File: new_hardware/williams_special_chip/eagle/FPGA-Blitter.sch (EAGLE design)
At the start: 3 parts

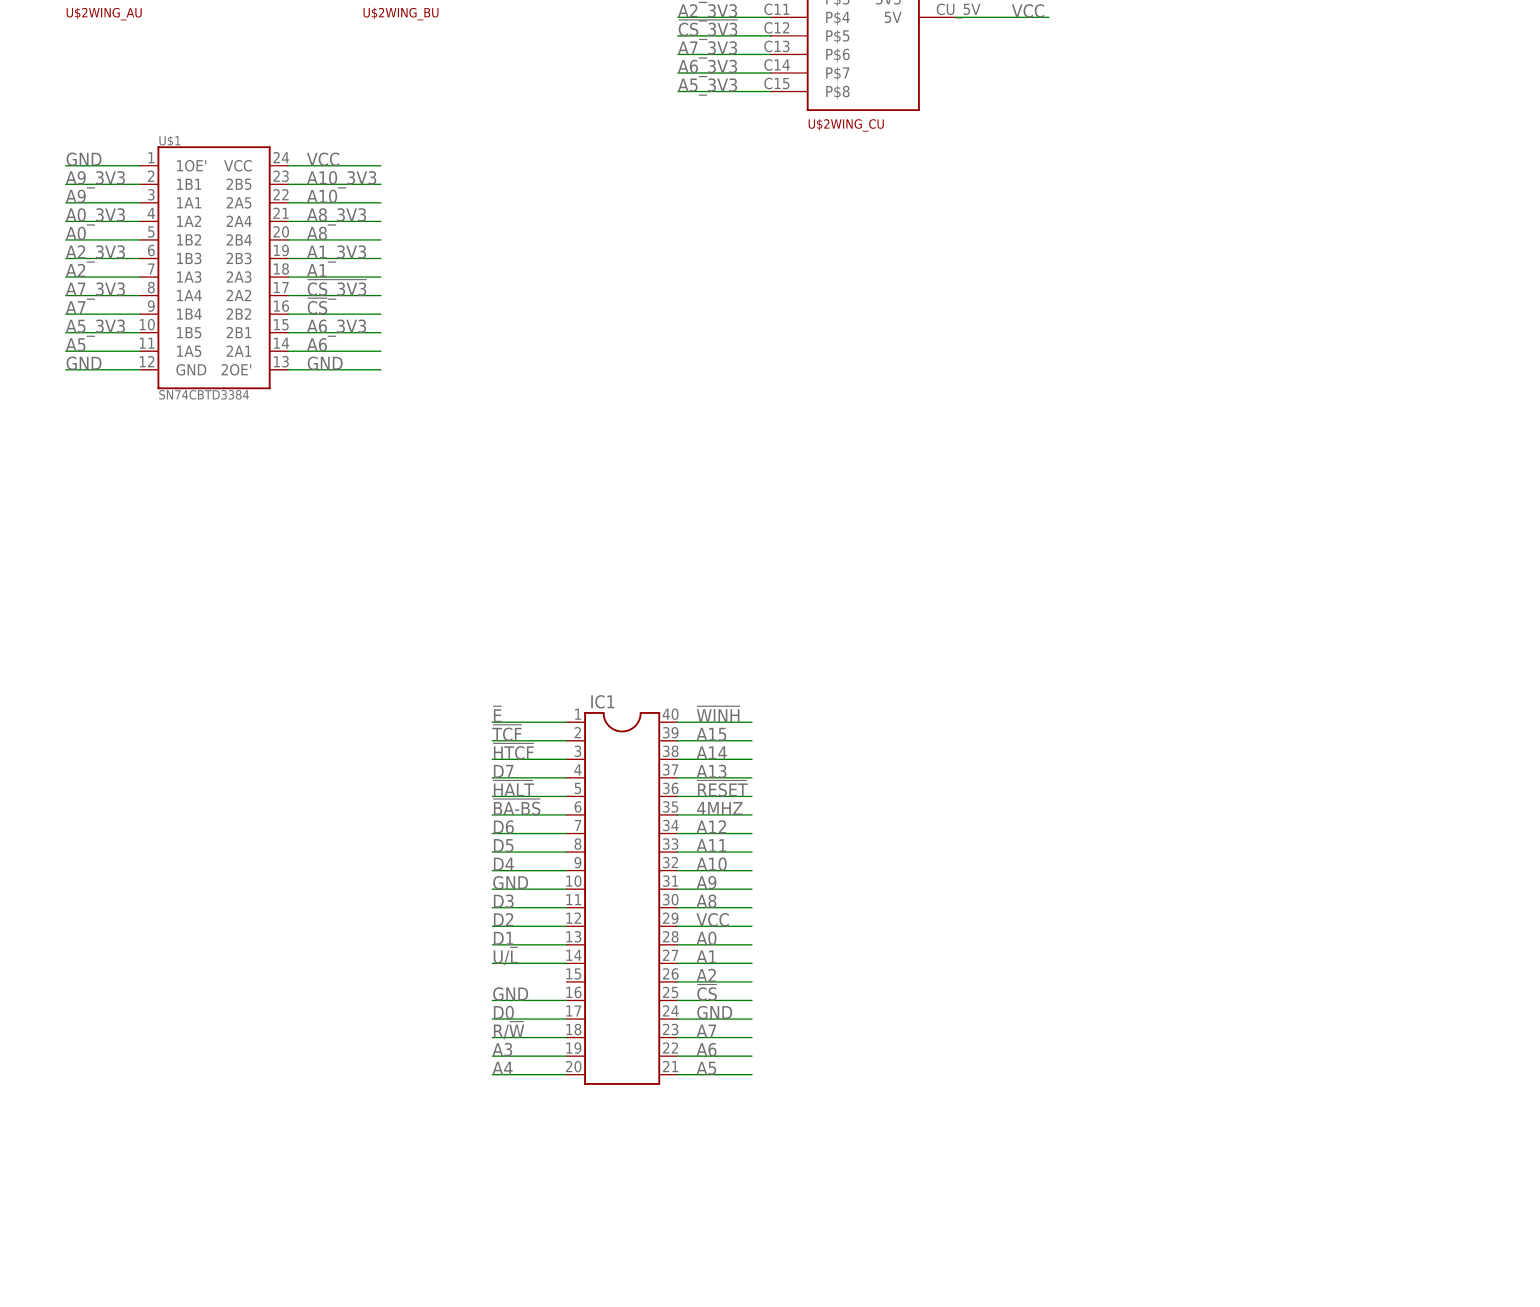
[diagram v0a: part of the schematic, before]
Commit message: added 20 I/O line quickswitch part.  about to try auto-router
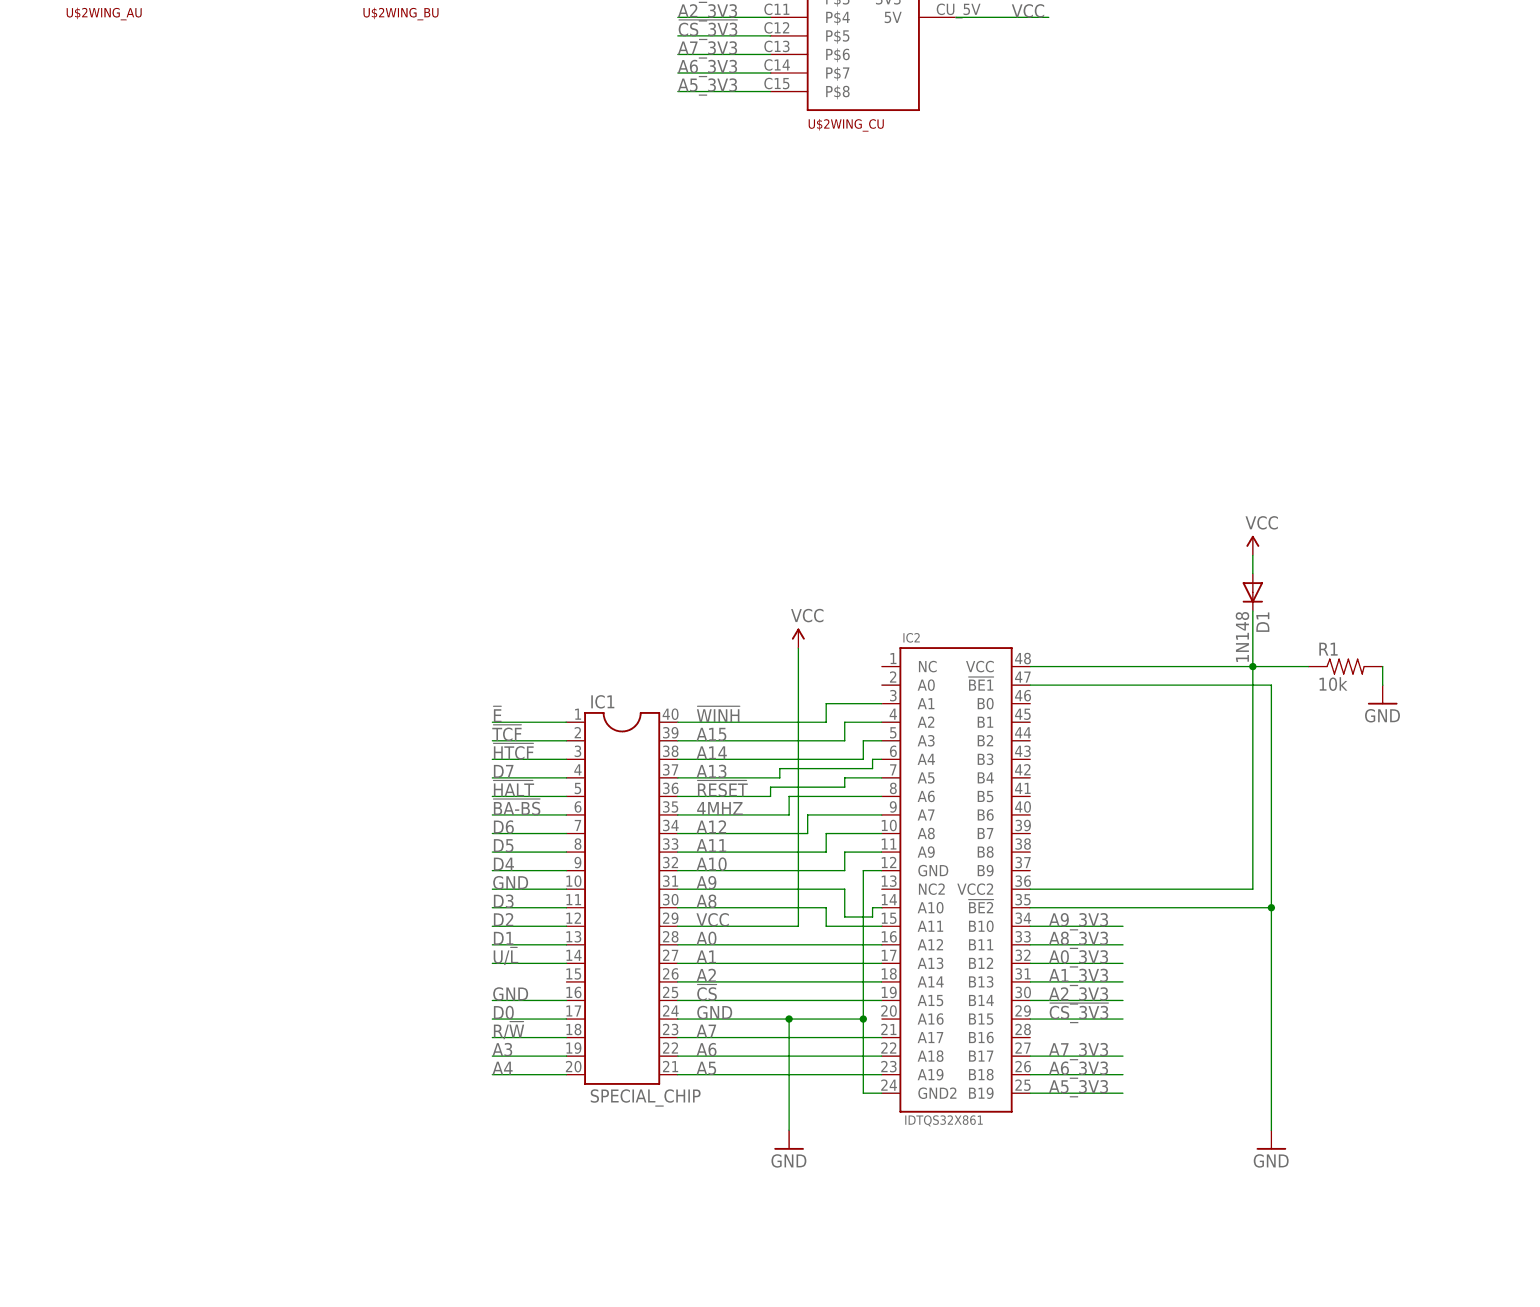
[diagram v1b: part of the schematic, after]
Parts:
- removed U$1: SN74CBTD3384, mpo:SN74CBTD3384
- added D1: 1N148, SparkFun:DIODE1N4148
- added IC2: IDTQS32X861, mpo:IDTQS32X861
- added R1: 10k, SparkFun:RESISTOR1206
- IC1: value (none) -> SPECIAL_CHIP
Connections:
- removed net A10_3V3: U$1.2B5
- new net N$8: D1.C, IC2.VCC, IC2.VCC2, R1.1
- net !CS: now also IC2.A15; no longer U$1.2B2
- net !CS_3V3: now also IC2.B15; no longer U$1.2A2
- net !RESET: now also IC2.A5
- net !WINH: now also IC2.A1
- net 4MHZ: now also IC2.A6
- net A0: now also IC2.A12; no longer U$1.1B2
- net A0_3V3: now also IC2.B12; no longer U$1.1A2
- net A1: now also IC2.A13; no longer U$1.2A3
- net A10: now also IC2.A9; no longer U$1.2A5
- net A11: now also IC2.A8
- net A12: now also IC2.A7
- net A13: now also IC2.A4
- net A14: now also IC2.A3
- net A15: now also IC2.A2
- net A1_3V3: now also IC2.B13; no longer U$1.2B3
- net A2: now also IC2.A14; no longer U$1.1A3
- net A2_3V3: now also IC2.B14; no longer U$1.1B3
- net A5: now also IC2.A19; no longer U$1.1A5
- net A5_3V3: now also IC2.B19; no longer U$1.1B5
- net A6: now also IC2.A18; no longer U$1.2A1
- net A6_3V3: now also IC2.B18; no longer U$1.2B1
- net A7: now also IC2.A17; no longer U$1.1B4
- net A7_3V3: now also IC2.B17; no longer U$1.1A4
- net A8: now also IC2.A11; no longer U$1.2B4
- net A8_3V3: now also IC2.B11; no longer U$1.2A4
- net A9: now also IC2.A10; no longer U$1.1A1
- net A9_3V3: now also IC2.B10; no longer U$1.1B1
- net GND: now also IC2.!BE1, IC2.!BE2, IC2.GND, IC2.GND2, R1.2; no longer U$1.1OE', U$1.2OE', U$1.GND
- net VCC: now also D1.A; no longer U$1.VCC
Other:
- note added: "Goal: Make VCC into IC2 be about 4.3V"

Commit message: got one half finished
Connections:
- new net A10_3V3: IC2.B9, U$2WING_CL.P$8
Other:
- moved on the sheet: U$2WING_CL
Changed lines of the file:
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@@
 <setting verticaltext="up"/>
 </settings>
-<grid distance="0.1" unitdist="inch" unit="inch" style="lines" multiple="1" display="no" altdistance="0.05" altunitdist="inch" altunit="inch"/>
+<grid distance="0.1" unitdist="inch" unit="inch" style="lines" multiple="1" display="no" altdistance="0.01" altunitdist="inch" altunit="inch"/>
 <layers>
 <layer number="1" name="Top" color="4" fill="1" visible="no" active="no"/>
@@
 <instance part="U$2" gate="WING_BL" x="-30.48" y="187.96"/>
 <instance part="U$2" gate="WING_BU" x="-30.48" y="157.48"/>
-<instance part="U$2" gate="WING_CL" x="10.16" y="187.96"/>
+<instance part="U$2" gate="WING_CL" x="30.48" y="187.96"/>
 <instance part="U$2" gate="WING_CU" x="30.48" y="142.24"/>
 <instance part="IC2" gate="G$1" x="45.72" y="45.72"/>
@@
 <segment>
 <pinref part="U$2" gate="WING_CL" pin="5V"/>
-<wire x1="30.48" y1="180.34" x2="43.18" y2="180.34" width="0.1524" layer="91"/>
+<wire x1="50.8" y1="180.34" x2="63.5" y2="180.34" width="0.1524" layer="91"/>
 </segment>
 </net>
@@
 </segment>
 </net>
+<net name="A10_3V3" class="0">
+<segment>
+<pinref part="IC2" gate="G$1" pin="B9"/>
+<wire x1="60.96" y1="17.78" x2="73.66" y2="17.78" width="0.1524" layer="91"/>
+<label x="63.5" y="17.78" size="1.778" layer="95"/>
+</segment>
+<segment>
+<pinref part="U$2" gate="WING_CL" pin="P$8"/>
+<wire x1="25.4" y1="170.18" x2="12.7" y2="170.18" width="0.1524" layer="91"/>
+<label x="12.7" y="170.18" size="1.778" layer="95"/>
+</segment>
+</net>

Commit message: gotta just verify pins chosen and this is ready for production
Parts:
- added D2: 1N148, SparkFun:DIODE1N4148
- added IC3, IC4: IDTQS3861, mpo:IDTQS3861
- added R2: 10k, SparkFun:RESISTOR1206
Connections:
- removed net N$1: U$2WING_AL.5V
- removed net N$2: U$2WING_AU.5V
- removed net N$3: U$2WING_BL.5V
- new net !BA-BS_3V3: IC3.A6, U$2WING_BL.P$5
- new net !HALT_3V3: IC3.A5, U$2WING_BL.P$4
- new net !HTCF_3V3: IC3.A3, U$2WING_BL.P$2
- new net !RESET_3V3: IC2.B5, U$2WING_CL.P$4
- new net !TCF_3V3: IC3.A2, U$2WING_BL.P$1
- new net !WINH_3V3: IC2.B1, U$2WING_AU.P$8
- new net 4MHZ_3V3: IC2.B6, U$2WING_CL.P$5
- new net A11_3V3: IC2.B8, U$2WING_CL.P$7
- new net A12_3V3: IC2.B7, U$2WING_CL.P$6
- new net A13_3V3: IC2.B4, U$2WING_CL.P$3
- new net A14_3V3: IC2.B3, U$2WING_CL.P$2
- new net A15_3V3: IC2.B2, U$2WING_CL.P$1
- new net A3_3V3: IC4.A8, U$2WING_BU.P$7
- new net A4_3V3: IC4.A9, U$2WING_BU.P$8
- new net D0_3V3: IC4.A6, U$2WING_BU.P$5
- new net D1_3V3: IC4.A2, U$2WING_BU.P$3
- new net D2_3V3: IC4.A1, U$2WING_BU.P$2
- new net D3_3V3: IC4.A0, U$2WING_BU.P$1
- new net D4_3V3: IC3.A9, U$2WING_BL.P$8
- new net D5_3V3: IC3.A8, U$2WING_BL.P$7
- new net D6_3V3: IC3.A7, U$2WING_BL.P$6
- new net D7_3V3: IC3.A4, U$2WING_BL.P$3
- new net E_3V3: IC3.A1, U$2WING_AU.P$7
- new net N$4: D2.C, IC3.VCC, IC4.VCC, R2.1
- new net R/!W_3V3: IC4.A7, U$2WING_BU.P$6
- new net U/!L_3V3: IC4.A3, U$2WING_BU.P$4
- net !BA-BS: now also IC3.B6
- net !E: now also IC3.B1
- net !HALT: now also IC3.B5
- net !HTCF: now also IC3.B3
- net !TCF: now also IC3.B2
- net A3: now also IC4.B8
- net A4: now also IC4.B9
- net D0: now also IC4.B6
- net D1: now also IC4.B2
- net D2: now also IC4.B1
- net D3: now also IC4.B0
- net D4: now also IC3.B9
- net D5: now also IC3.B8
- net D6: now also IC3.B7
- net D7: now also IC3.B4
- net GND: now also IC3.BE', IC3.GND, IC4.BE', IC4.GND, R2.2
- net R/!W: now also IC4.B7
- net U/!L: now also IC4.B3
- net VCC: now also D2.A
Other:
- note added: "Goal: Make VCC be about 4.3V"
- note removed: "Goal: Make VCC into IC2 be about 4.3V"
- moved on the sheet: U$2WING_AL, U$2WING_AU, U$2WING_BL, U$2WING_BU

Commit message: added note about current
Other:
- note added: "Each IDTQS IC can output 120 mA, so make sure diode can handle that (if it is used for something beyond a voltage reference, which I am not sure about)"
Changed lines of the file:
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@@
 <text x="96.52" y="55.88" size="1.778" layer="98">Goal: Make VCC be about 4.3V</text>
 <text x="-35.56" y="68.58" size="1.778" layer="98">Goal: Make VCC be about 4.3V</text>
+<text x="12.7" y="81.28" size="1.778" layer="98">Each IDTQS IC can output 120 mA,
+so make sure diode can handle that
+(if it is used for something beyond a voltage
+reference, which I am not sure about)</text>
 </plain>
 <instances>
@@
 </schematic>
 </drawing>
+<compatibility>
+<note version="6.3" minversion="6.2.2" severity="warning">
+Since Version 6.2.2 text objects can contain more than one line,
+which will not be processed correctly with this version.
+</note>
+</compatibility>
 </eagle>

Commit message: tweaks
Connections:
- removed net E_3V3: IC3.A1, U$2WING_AU.P$7
- removed net N$5: U$2WING_CL.5V
- new net !E_3V3: IC3.A1, U$2WING_AU.P$6
- net !RESET_3V3: now also U$2WING_CL.P$3; no longer U$2WING_CL.P$4
- net !WINH_3V3: now also U$2WING_AU.P$7; no longer U$2WING_AU.P$8
- net 4MHZ_3V3: now also U$2WING_CL.P$4; no longer U$2WING_CL.P$5
- net A10_3V3: now also U$2WING_CL.P$7; no longer U$2WING_CL.P$8
- net A11_3V3: now also U$2WING_CL.P$6; no longer U$2WING_CL.P$7
- net A12_3V3: now also U$2WING_CL.P$5; no longer U$2WING_CL.P$6
- net A13_3V3: now also U$2WING_CL.P$2; no longer U$2WING_CL.P$3
- net A14_3V3: now also U$2WING_CL.P$1; no longer U$2WING_CL.P$2
- net A15_3V3: now also U$2WING_AU.P$8; no longer U$2WING_CL.P$1
- net A9_3V3: now also U$2WING_CL.P$8
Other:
- note added: "where is A9?"
- moved on the sheet: U$2WING_AU, U$2WING_CL
